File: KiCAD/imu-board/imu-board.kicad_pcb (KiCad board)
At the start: 4 copper layers, 16 x 8 mm, 10 parts, among them J1 Conn_01x04, J3 AVR-ISP-6, U2 ISM330DHCX, U3 ATmega168A-MM

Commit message: Candidate V2 layout
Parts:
- removed J1: Conn_01x04, Connector_PinHeader_1.27mm:PinHeader_1x04_P1.27mm_Vertical
- added J2: A-2004-3-4-LP-N-R, my_RJ:A-2004-3-4-LP, B.Cu at (54.1, 71.5)
- C1, C2: value C_Small -> 0.1uF
- J3: value AVR-ISP-6 -> -OMIT-
- JP1, JP2: value JPR2 -> -OMIT-
- R1: value R_US -> 680
- U3: footprint Package_DFN_QFN:QFN-28-1EP_4x4mm_P0.45mm_EP2.4x2.4mm -> my_AVR:QFN-28-1EP_4x4mm_P0.45mm_EP2.4x2.4mm
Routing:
- net /TXD: track 8.40 -> 18.8 mm
- net /RXD: track 10.3 -> 17.2 mm
- net /nRESET: track 7.37 -> 7.98 mm
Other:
- board size 16 x 8 mm -> 12.1 x 20.3 mm
- board text added: "NN IMU V2.0 1/25"

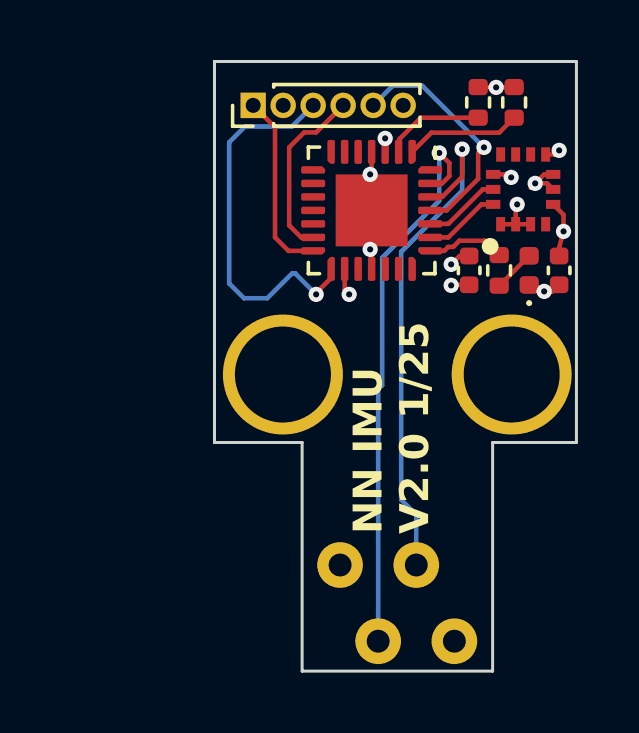
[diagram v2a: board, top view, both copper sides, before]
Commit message: working on even smaller version
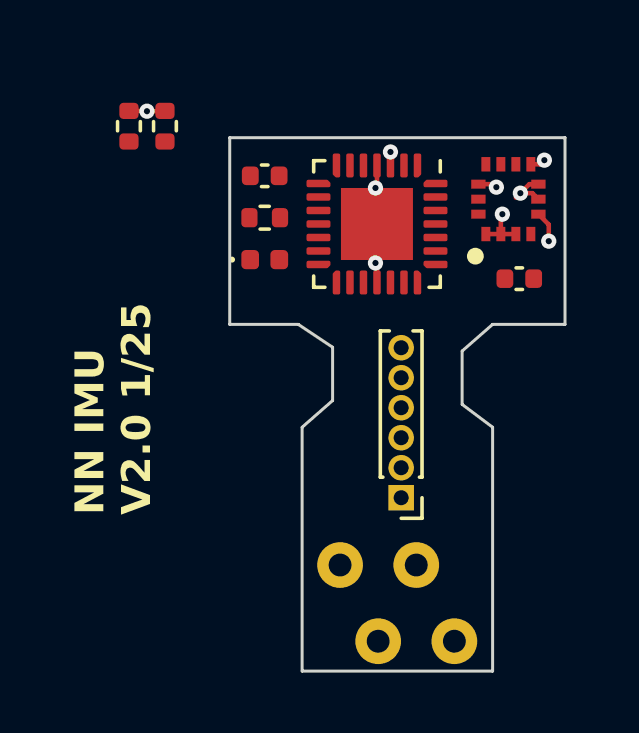
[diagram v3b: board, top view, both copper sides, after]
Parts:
- moved J3 14.0 mm to (56.1, 69.3), turned to 180 degrees
- moved JP1 11.7 mm to (47.1, 56.9)
- moved JP2 11.7 mm to (48.3, 56.9)
- moved D1 8.82 mm to (51.6, 61.3), turned to 0 degrees
- moved R1 8.01 mm to (51.6, 59.9), turned to 0 degrees
- moved C2 7.51 mm to (51.6, 58.5), turned to 0 degrees
- moved C1 1.36 mm to (60.1, 62.0), turned to 180 degrees
- moved U2 0.59 mm to (59.7, 59.3)
- moved U3 0.49 mm to (55.3, 60.2)
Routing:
- net /TXD: track 18.8 -> 0.00 mm, vias 1 -> 0
- net /RXD: track 17.2 -> 0.00 mm, vias 1 -> 0
- net /SCK: track 12.5 -> 0.00 mm, vias 1 -> 0
- net /nRESET: track 7.98 -> 0.00 mm, vias 1 -> 0
- net /MISO: track 6.16 -> 0.00 mm
- net /MOSI: track 5.95 -> 0.00 mm
- net Net-(JP2-A): track 3.87 -> 0.00 mm
- net Net-(JP1-A): track 3.36 -> 0.00 mm
- net Net-(U3-PC3): track 2.64 -> 0.00 mm
- net /SCL: track 2.58 -> 0.00 mm
- net /SDA: track 2.56 -> 0.00 mm
- net VCC: track 5.41 -> 2.94 mm, vias 6 -> 4
- net GND: track 10.1 -> 8.45 mm, vias 7 -> 5
- net Net-(D1-A): track 1.41 -> 0.00 mm
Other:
- board size 12.1 x 20.3 mm -> 11.2 x 17.8 mm
- board text removed: "FNIRS IMU V1.0 1/2024 ESH"
